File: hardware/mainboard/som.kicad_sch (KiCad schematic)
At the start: 24 parts

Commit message: Design updates
Signed-off-by: gatecat <gatecat@ds0.me>
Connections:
- net JTAG_TDI: no longer SOM?.1A23 (JTAG_TDO_M2C)
- net CSI1_D3+: now reaches SOM?.2A32 (HPC19_P)
- net CSI1_D3-: now reaches SOM?.2A33 (HPC19_N)
- net CSI1_CLK+: now reaches SOM?.2A38 (HPC15_CC_P)
- net CSI1_CLK-: now reaches SOM?.2A39 (HPC15_CC_N)
- net CSI1_D0+: now reaches SOM?.2B33 (HPC16_P)
- net CSI1_D0-: now reaches SOM?.2B34 (HPC16_N)
- net CSI1_D2+: now reaches SOM?.2B39 (HPC18_P)
- net CSI1_D2-: now reaches SOM?.2B40 (HPC18_N)
- net CSI1_D1+: now reaches SOM?.2C26 (HPC17_P)
- net CSI1_D1-: now reaches SOM?.2C27 (HPC17_N)
- net RIGHT_LCD_~{RST}: now reaches SOM?.2C46 (HDB06)
- net CAM_R_SDA: now reaches SOM?.2C50 (HDB09)
- net CAM_R_SCL: now reaches SOM?.2C51 (HDB10)
- net RIGHT_LCD_TE: now reaches SOM?.2C52 (HDB11)
- net UART_TX: now reaches SOM?.1B29 (MIO36)
- net UART_RX: now reaches SOM?.1B30 (MIO37)
- net FRONT_LCD_TE renamed LEFT_LCD_TE
- net FRONT_LCD_~{RST} renamed LEFT_LCD_~{RST}
- net FRONT_SCL renamed CAM_L_SCL
- net FRONT_SDA renamed CAM_L_SDA
- new net JTAG_TDO: SOM?.1A23 (JTAG_TDO_M2C)
- no-connect marks 126 -> 121

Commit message: Re-add USB-C PD control
Signed-off-by: gatecat <gatecat@ds0.me>
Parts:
- removed C? (x2): 100n, Capacitor_SMD:C_0402_1005Metric, symbol Device:C_Small
- removed U?: CP3225-125.000-3.3-25-X-T-TR, Oscillator:Oscillator_SMD_IDT_JS6-6_5.0x3.2mm_P1.27mm, symbol Oscillator:XUX52
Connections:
- net MAG_SDA: now reaches SOM?.2C58 (HDC09)
- net MAG_SCL: now reaches SOM?.2C59 (HDC10)
- net IO_I2C_SCL renamed PD_I2C_SCL
- net IO_I2C_SDA renamed PD_I2C_SDA
- net IO_INT renamed PD_INT
- net REFCLK125+: no longer names the net of SOM?.1A51 (GTR_REFCLK3_C2M_P)
- net REFCLK125-: no longer names the net of SOM?.1A52 (GTR_REFCLK3_C2M_N)
- net RIGHT_DET renamed USBC_SEL
- no-connect marks 121 -> 124
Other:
- moved on the sheet: C?, U?

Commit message: ERC fixes
Signed-off-by: gatecat <gatecat@ds0.me>
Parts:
- removed FB?: Ferrite_Bead_Small, Inductor_SMD:L_0603_1608Metric, symbol Device:Ferrite_Bead_Small
- added FB1: FerriteBead_Small, symbol Device:FerriteBead_Small
- added R2: 10k, symbol Device:R_Small
- gave numbers to parts that had none: 13
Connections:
- net +3V3PS: now also FB1.1
- net 3V3_OSC: now also FB1.2
- net PERST_IN: now reaches SOM1.1B28 (MIO35_WD_OUT)
- net PERST_IN: now also R2.2
- net BTN0: now reaches SOM1.1B44 (MIO70)
- net BTN1: now reaches SOM1.1B45 (MIO71)
- net BTN2: now reaches SOM1.1B46 (MIO72)
- net BTN3: now reaches SOM1.1A42 (MIO73)
- net DP_OUT_L0+: no longer names the net of SOM1.2D9 (GTH_DP0_M2C_P)
- net DP_OUT_L0-: no longer names the net of SOM1.2D10 (GTH_DP0_M2C_N)
- net DP_OUT_L1+: no longer names the net of SOM1.2C7 (GTH_DP1_M2C_P)
- net DP_OUT_L1-: no longer names the net of SOM1.2C8 (GTH_DP1_M2C_N)
- net DP_OUT_L2+: no longer names the net of SOM1.2B5 (GTH_DP2_M2C_P)
- net DP_OUT_L2-: no longer names the net of SOM1.2B6 (GTH_DP2_M2C_N)
- net DP_OUT_L3+: no longer names the net of SOM1.2A3 (GTH_DP3_M2C_P)
- net DP_OUT_L3-: no longer names the net of SOM1.2A4 (GTH_DP3_2C_N)
- net FRONT_LED0: no longer names the net of SOM1.2C54 (HDC06)
- net FRONT_LED1 renamed DP_HPD
- new net +1V8PS: R2.1
- no-connect marks 124 -> 147

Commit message: Add some footprint mappings
Signed-off-by: gatecat <gatecat@ds0.me>
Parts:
- C1: footprint Capacitor_SMD:C_0805_2012Metric -> Capacitor_SMD:C_1206_3216Metric
- FB1: footprint (none) -> Inductor_SMD:L_0603_1608Metric
- R2: footprint (none) -> Resistor_SMD:R_0402_1005Metric
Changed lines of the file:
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@@
     (property "Reference" "R2" (id 0) (at 129.54 85.09 90))
     (property "Value" "10k" (id 1) (at 129.54 87.63 90))
-    (property "Footprint" "" (id 2) (at 129.54 91.44 0)
+    (property "Footprint" "Resistor_SMD:R_0402_1005Metric" (id 2) (at 129.54 91.44 0)
       (effects (font (size 1.27 1.27)) hide)
     )
@@
       (effects (font (size 1.27 1.27)) (justify left))
     )
-    (property "Footprint" "Capacitor_SMD:C_0805_2012Metric" (id 2) (at 347.98 147.32 0)
+    (property "Footprint" "Capacitor_SMD:C_1206_3216Metric" (id 2) (at 347.98 147.32 0)
       (effects (font (size 1.27 1.27)) hide)
     )
@@
       (effects (font (size 1.27 1.27)) (justify left))
     )
-    (property "Footprint" "" (id 2) (at 380.492 134.62 90)
-      (effects (font (size 1.27 1.27)) hide)
-    )
+    (property "Footprint" "Inductor_SMD:L_0603_1608Metric" (id 2) (at 380.492 134.62 90)
+      (effects (font (size 1.27 1.27)) hide)
+    )

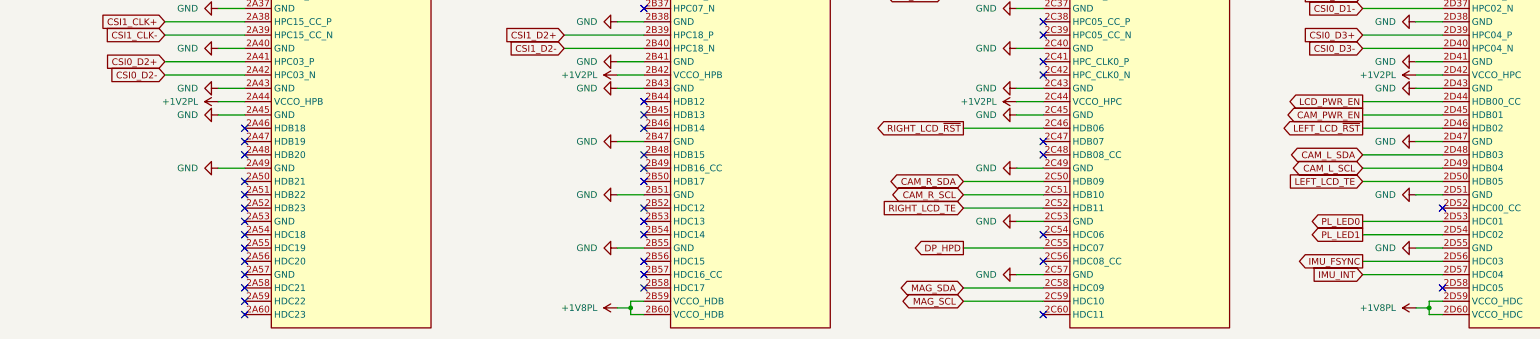
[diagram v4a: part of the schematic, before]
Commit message: Rework power arch to add 3V3PL; 5x PL RGB LEDs
Signed-off-by: gatecat <gatecat@ds0.me>
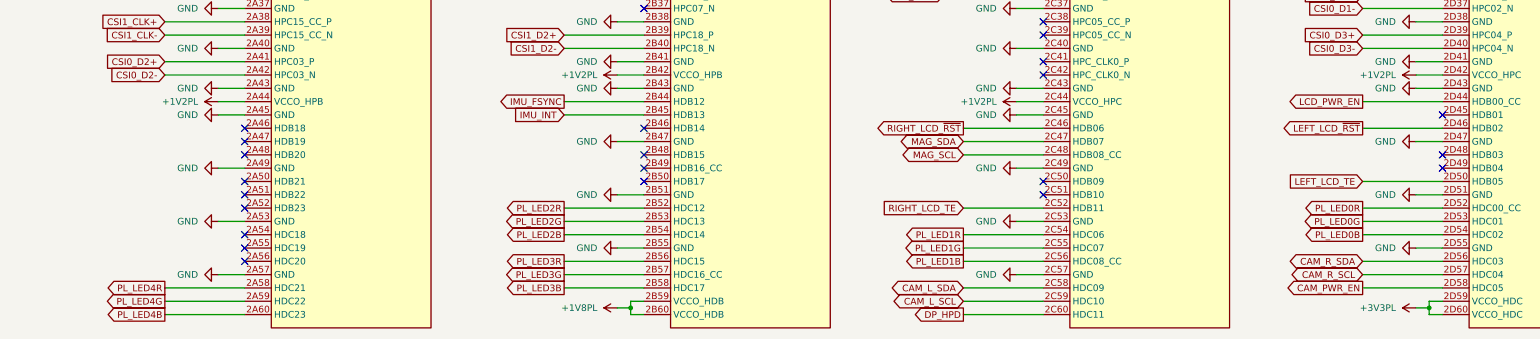
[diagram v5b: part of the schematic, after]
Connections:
- net +1V8PL: no longer SOM1.2D59 (VCCO_HDC), SOM1.2D60 (VCCO_HDC)
- net +3V3PS: now also SOM1.2D59 (VCCO_HDC), SOM1.2D60 (VCCO_HDC)
- net CAM_L_SCL: now also SOM1.2C59 (HDC10); no longer SOM1.2D49 (HDB04)
- net CAM_L_SDA: now also SOM1.2C58 (HDC09); no longer SOM1.2D48 (HDB03)
- net CAM_PWR_EN: now also SOM1.2D58 (HDC05); no longer SOM1.2D45 (HDB01)
- net CAM_R_SCL: now also SOM1.2D57 (HDC04); no longer SOM1.2C51 (HDB10)
- net CAM_R_SDA: now also SOM1.2D56 (HDC03); no longer SOM1.2C50 (HDB09)
- net DP_HPD: now also SOM1.2C60 (HDC11); no longer SOM1.2C55 (HDC07)
- net GND: now also SOM1.2A53 (GND), SOM1.2A57 (GND)
- net IMU_FSYNC: now also SOM1.2B44 (HDB12); no longer SOM1.2D56 (HDC03)
- net IMU_INT: now also SOM1.2B45 (HDB13); no longer SOM1.2D57 (HDC04)
- net MAG_SCL: now also SOM1.2C48 (HDB08_CC); no longer SOM1.2C59 (HDC10)
- net MAG_SDA: now also SOM1.2C47 (HDB07); no longer SOM1.2C58 (HDC09)
- net PL_LED4R: now reaches SOM1.2A58 (HDC21)
- net PL_LED4G: now reaches SOM1.2A59 (HDC22)
- net PL_LED4B: now reaches SOM1.2A60 (HDC23)
- net PL_LED2R: now reaches SOM1.2B52 (HDC12)
- net PL_LED2G: now reaches SOM1.2B53 (HDC13)
- net PL_LED2B: now reaches SOM1.2B54 (HDC14)
- net PL_LED3R: now reaches SOM1.2B56 (HDC15)
- net PL_LED3G: now reaches SOM1.2B57 (HDC16_CC)
- net PL_LED3B: now reaches SOM1.2B58 (HDC17)
- net PL_LED1R: now reaches SOM1.2C54 (HDC06)
- net PL_LED1B: now reaches SOM1.2C56 (HDC08_CC)
- net PL_LED0R: now reaches SOM1.2D52 (HDC00_CC)
- net PL_LED0 renamed PL_LED0G
- net PL_LED1 renamed PL_LED0B
- new net PL_LED1G: SOM1.2C55 (HDC07)
- no-connect marks 147 -> 132

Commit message: Add separate reg for 3V3PL
Signed-off-by: gatecat <gatecat@ds0.me>
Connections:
- net +3V3PS: no longer SOM1.2D59 (VCCO_HDC), SOM1.2D60 (VCCO_HDC)
- new net +3V3PL: SOM1.2D59 (VCCO_HDC), SOM1.2D60 (VCCO_HDC)

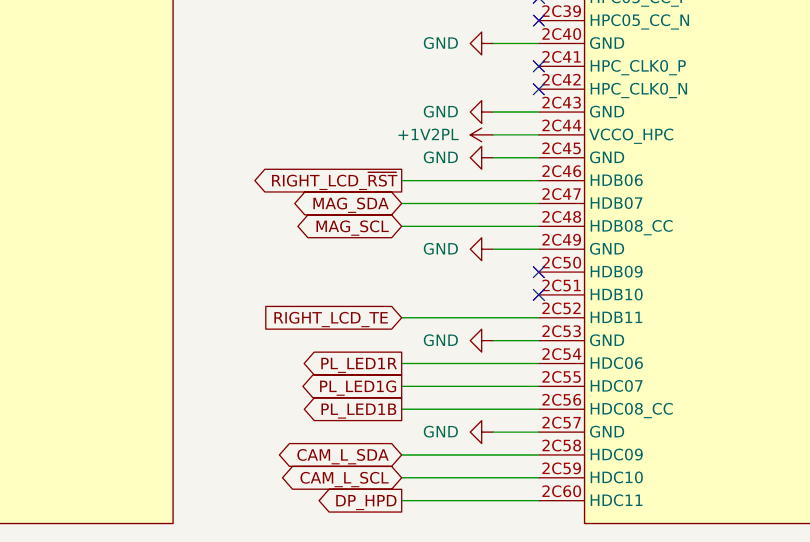
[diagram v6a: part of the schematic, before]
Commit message: Mechanical updates; add cam clk connectors
Signed-off-by: gatecat <gatecat@ds0.me>
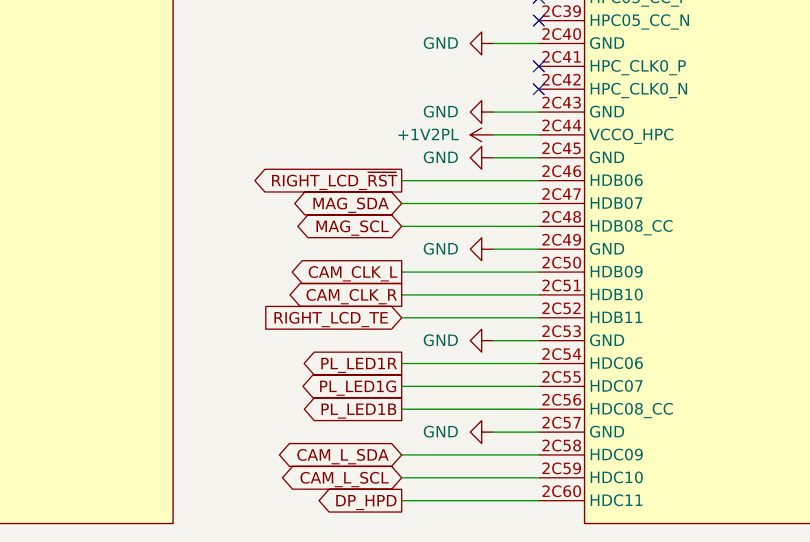
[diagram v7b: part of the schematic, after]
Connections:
- net CAM_CLK_L: now reaches SOM1.2C50 (HDB09)
- net CAM_CLK_R: now reaches SOM1.2C51 (HDB10)
- no-connect marks 132 -> 130
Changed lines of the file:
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@@
   (no_connect (at 77.47 266.7))
   (no_connect (at 229.87 215.9))
-  (no_connect (at 229.87 327.66))
   (no_connect (at 153.67 322.58))
   (no_connect (at 229.87 218.44))
@@
   (no_connect (at 153.67 276.86))
   (no_connect (at 153.67 254))
-  (no_connect (at 229.87 325.12))
   (no_connect (at 77.47 111.76))
   (no_connect (at 306.07 60.96))
@@
     (stroke (width 0) (type default) (color 0 0 0 0))
   )
+  (wire (pts (xy 214.63 327.66) (xy 229.87 327.66))
+    (stroke (width 0) (type default) (color 0 0 0 0))
+  )
   (wire (pts (xy 74.93 212.09) (xy 74.93 210.82))
     (stroke (width 0) (type default) (color 0 0 0 0))
@@
     (stroke (width 0) (type default) (color 0 0 0 0))
   )
+  (wire (pts (xy 214.63 325.12) (xy 229.87 325.12))
+    (stroke (width 0) (type default) (color 0 0 0 0))
+  )
   (wire (pts (xy 148.59 83.82) (xy 153.67 83.82))
     (stroke (width 0) (type default) (color 0 0 0 0))
@@
     )
   )
+  (global_label "CAM_CLK_R" (shape output) (at 214.63 327.66 180) (fields_autoplaced)
+    (effects (font (size 1.27 1.27)) (justify right))
+    (property "Intersheet References" "${INTERSHEET_REFS}" (id 0) (at 201.6336 327.5806 0)
+      (effects (font (size 1.27 1.27)) (justify right) hide)
+    )
+  )
   (global_label "SPI_SCLK" (shape output) (at 290.83 121.92 180) (fields_autoplaced)
     (effects (font (size 1.27 1.27)) (justify right))
@@
     )
   )
+  (global_label "CAM_CLK_L" (shape output) (at 214.63 325.12 180) (fields_autoplaced)
+    (effects (font (size 1.27 1.27)) (justify right))
+    (property "Intersheet References" "${INTERSHEET_REFS}" (id 0) (at 201.8755 325.0406 0)
+      (effects (font (size 1.27 1.27)) (justify right) hide)
+    )
+  )
   (global_label "SD_D2_1V8" (shape bidirectional) (at 214.63 109.22 180) (fields_autoplaced)
     (effects (font (size 1.27 1.27)) (justify right))
@@
     (pin "1B9")
   )
-  (symbol (lib_id "Device:C_Small") (at 397.51 151.13 90) (unit 1)
-    (in_bom yes) (on_board yes) (fields_autoplaced)
-    (property "Reference" "C5" (id 0) (at 397.51 145.6014 90))
-    (property "Value" "100n" (id 1) (at 397.51 148.3765 90))
-    (property "Footprint" "Capacitor_SMD:C_0402_1005Metric" (id 2) (at 397.51 151.13 0)
-      (effects (font (size 1.27 1.27)) hide)
-    )
-    (property "Datasheet" "~" (id 3) (at 397.51 151.13 0)
-      (effects (font (size 1.27 1.27)) hide)
-    )
-    (pin "1")
-    (pin "2")
-  )
   (symbol (lib_id "power:GND") (at 224.79 261.62 270) (unit 1)
     (in_bom yes) (on_board yes) (fields_autoplaced)
@@
     (pin "1")
   )
+  (symbol (lib_id "Device:C_Small") (at 397.51 151.13 90) (unit 1)
+    (in_bom yes) (on_board yes) (fields_autoplaced)
+    (property "Reference" "C5" (id 0) (at 397.51 145.6014 90))
+    (property "Value" "100n" (id 1) (at 397.51 148.3765 90))
+    (property "Footprint" "Capacitor_SMD:C_0402_1005Metric" (id 2) (at 397.51 151.13 0)
+      (effects (font (size 1.27 1.27)) hide)
+    )
+    (property "Datasheet" "~" (id 3) (at 397.51 151.13 0)
+      (effects (font (size 1.27 1.27)) hide)
+    )
+    (pin "1")
+    (pin "2")
+  )
   (symbol (lib_id "Device:FerriteBead_Small") (at 382.27 134.62 0) (unit 1)

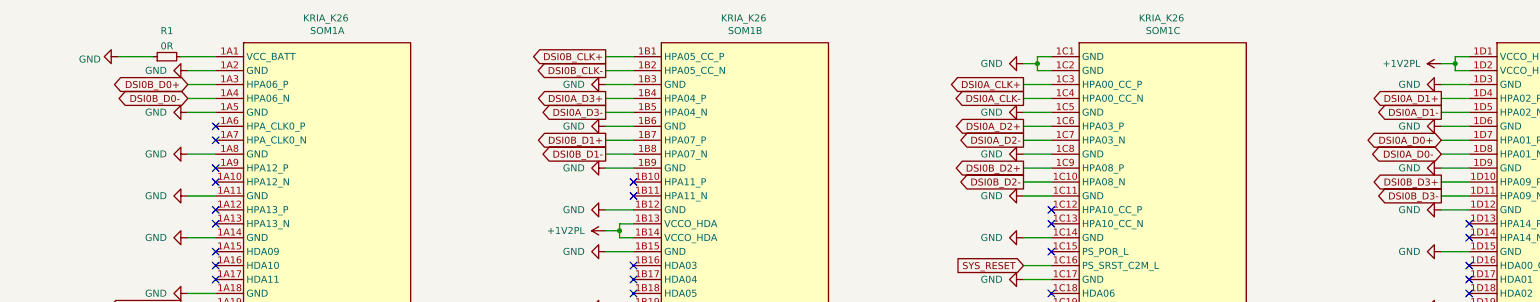
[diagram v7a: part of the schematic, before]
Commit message: Begin some routing
Signed-off-by: gatecat <gatecat@ds0.me>
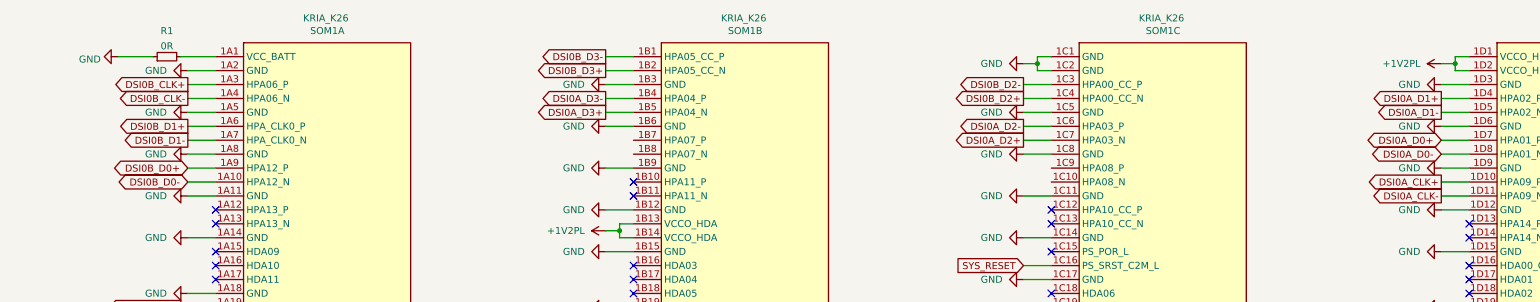
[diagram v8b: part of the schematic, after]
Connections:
- net DSI0A_CLK+: now also SOM1.1D10 (HPA09_P); no longer SOM1.1C3 (HPA00_CC_P)
- net DSI0A_CLK-: now also SOM1.1D11 (HPA09_N); no longer SOM1.1C4 (HPA00_CC_N)
- net DSI0A_D2+: now also SOM1.1C7 (HPA03_N); no longer SOM1.1C6 (HPA03_P)
- net DSI0A_D2-: now also SOM1.1C6 (HPA03_P); no longer SOM1.1C7 (HPA03_N)
- net DSI0A_D3+: now also SOM1.1B5 (HPA04_N); no longer SOM1.1B4 (HPA04_P)
- net DSI0A_D3-: now also SOM1.1B4 (HPA04_P); no longer SOM1.1B5 (HPA04_N)
- net DSI0B_CLK+: now also SOM1.1A3 (HPA06_P); no longer SOM1.1B1 (HPA05_CC_P)
- net DSI0B_CLK-: now also SOM1.1A4 (HPA06_N); no longer SOM1.1B2 (HPA05_CC_N)
- net DSI0B_D0+: now also SOM1.1A9 (HPA12_P); no longer SOM1.1A3 (HPA06_P)
- net DSI0B_D0-: now also SOM1.1A10 (HPA12_N); no longer SOM1.1A4 (HPA06_N)
- net DSI0B_D1+: now also SOM1.1A6 (HPA_CLK0_P); no longer SOM1.1B7 (HPA07_P)
- net DSI0B_D1-: now also SOM1.1A7 (HPA_CLK0_N); no longer SOM1.1B8 (HPA07_N)
- net DSI0B_D2+: now also SOM1.1C4 (HPA00_CC_N); no longer SOM1.1C9 (HPA08_P)
- net DSI0B_D2-: now also SOM1.1C3 (HPA00_CC_P); no longer SOM1.1C10 (HPA08_N)
- net DSI0B_D3+: now also SOM1.1B2 (HPA05_CC_N); no longer SOM1.1D10 (HPA09_P)
- net DSI0B_D3-: now also SOM1.1B1 (HPA05_CC_P); no longer SOM1.1D11 (HPA09_N)
- no-connect marks 130 -> 126
